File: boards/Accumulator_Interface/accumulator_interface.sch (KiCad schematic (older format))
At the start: 12 parts, among them J1 INTERNAL, J10 AIR_CTRL_18, J2 EXTERNAL, J3 AIR_CTRL, J4 IMD_LATCH, J5 DISCHARGE, J6 BMS_Master, J7 BMS, J8 TSAL/AIL, J9 IMD_LATCH, U1 RJ45_VT_AIR, U2 RJ45_VT_BMS

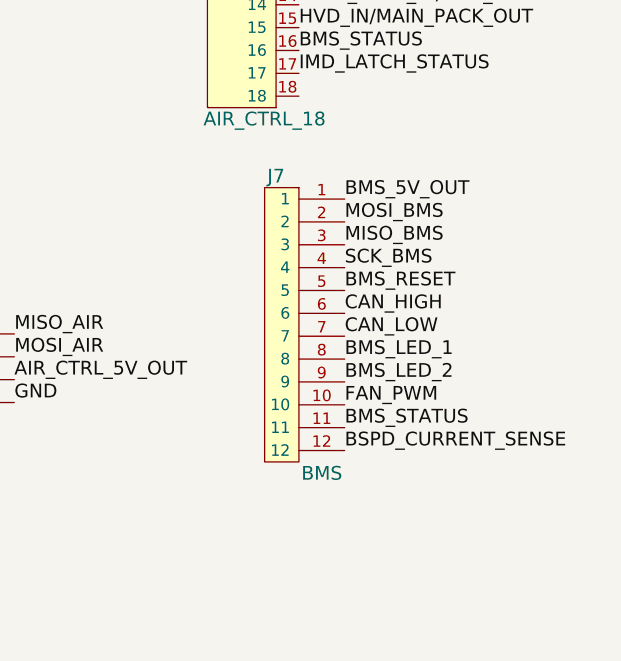
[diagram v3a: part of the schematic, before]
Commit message: added traces to accumulator
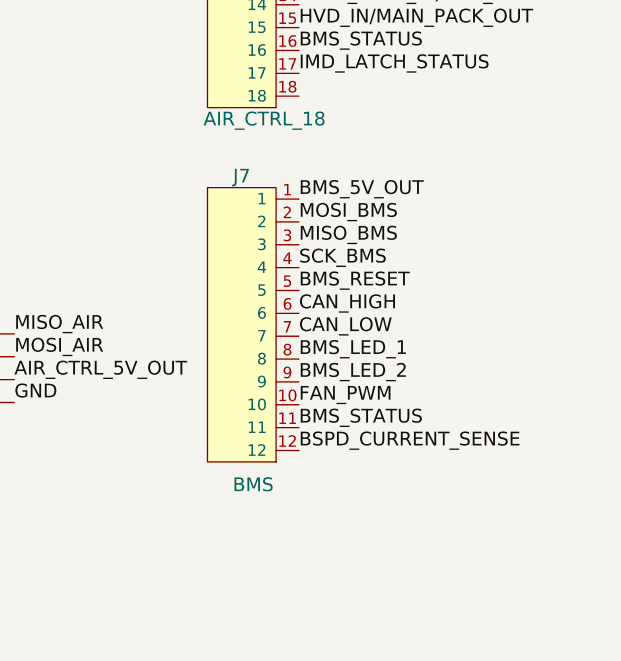
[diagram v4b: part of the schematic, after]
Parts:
- removed J7: BMS, symbol MicroFit_12
- added J7: BMS, footprints:micromatch_female_vert_12, symbol micromatch_female_TOP_ENTRY_locking_12
- J2: footprint (none) -> footprints:Ampseal_35
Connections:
- net BMS_5V_OUT: now also J7.1
- net BMS_LED_1: now also J7.8
- net BMS_LED_2: now also J7.9
- net BMS_RESET: now also J7.5
- net BMS_STATUS: now also J7.11
- net BSPD_CURRENT_SENSE: now also J7.12
- net CAN_HIGH: now also J7.6
- net CAN_LOW: now also J7.7
- net FAN_PWM: now also J7.10
- net MISO_BMS: now also J7.3
- net MOSI_BMS: now also J7.2
- net SCK_BMS: now also J7.4
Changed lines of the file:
@@
 F 0 "J2" H 750 5000 60  0000 C CNN
 F 1 "EXTERNAL" H 700 1400 60  0000 L CNN
-F 2 "" H 800 4550 60  0001 C CNN
+F 2 "footprints:Ampseal_35" H 800 4550 60  0001 C CNN
 F 3 "" H 800 4550 60  0001 C CNN
 	1    1000 3200
@@
 Text Label 5050 3850 0    60   ~ 0
 IMD_LATCH_STATUS
-Text Label 5250 4400 0    60   ~ 0
+Text Label 5050 4400 0    60   ~ 0
 BMS_5V_OUT
-Text Label 5250 4500 0    60   ~ 0
+Text Label 5050 4500 0    60   ~ 0
 MOSI_BMS
-Text Label 5250 4600 0    60   ~ 0
+Text Label 5050 4600 0    60   ~ 0
 MISO_BMS
-Text Label 5250 4700 0    60   ~ 0
+Text Label 5050 4700 0    60   ~ 0
 SCK_BMS
-Text Label 5250 4800 0    60   ~ 0
+Text Label 5050 4800 0    60   ~ 0
 BMS_RESET
-Text Label 5250 4900 0    60   ~ 0
-CAN_HIGH
-Text Label 5250 5000 0    60   ~ 0
-CAN_LOW
-Text Label 5250 5100 0    60   ~ 0
+Text Label 5050 4900 0    60   ~ 0
+CAN_HIGH
+Text Label 5050 5000 0    60   ~ 0
+CAN_LOW
+Text Label 5050 5100 0    60   ~ 0
 BMS_LED_1
-Text Label 5250 5200 0    60   ~ 0
+Text Label 5050 5200 0    60   ~ 0
 BMS_LED_2
-Text Label 5250 5300 0    60   ~ 0
-FAN_PWM
-Text Label 5250 5400 0    60   ~ 0
+Text Label 5050 5300 0    60   ~ 0
+FAN_PWM
+Text Label 5050 5400 0    60   ~ 0
 BMS_STATUS
-Text Label 5250 5500 0    60   ~ 0
+Text Label 5050 5500 0    60   ~ 0
 BSPD_CURRENT_SENSE
 Text Label 5050 1900 0    60   ~ 0
@@
 12V
 $Comp
-L MicroFit_12 J7
-U 1 1 5A7D1B20
-P 4700 4200
-F 0 "J7" H 4950 4100 60  0000 C CNN
-F 1 "BMS" H 5150 2800 60  0000 C CNN
-F 2 "" H 4700 4200 60  0001 C CNN
-F 3 "" H 4700 4200 60  0001 C CNN
-	1    4700 4200
-	1    0    0    -1
-$EndComp
+L micromatch_female_TOP_ENTRY_locking_12 J7
+U 1 1 5A825107
+P 4800 4950
+F 0 "J7" H 4800 5600 60  0000 C CNN
+F 1 "BMS" H 4850 4250 60  0000 C CNN
+F 2 "footprints:micromatch_female_vert_12" H 4700 5500 60  0001 C CNN
+F 3 "" H 4800 5600 60  0001 C CNN
+F 4 "https://www.digikey.com/product-detail/en/te-connectivity-amp-connectors/1-338068-2/A99503CT-ND/1955736" H 4900 5700 60  0001 C CNN "PurchasingLink"
+F 5 "Digi-Key" H 5000 5800 60  0001 C CNN "MFN"
+F 6 "A99503CT-ND" H 5000 6450 60  0001 C CNN "MPN"
+F 7 "Value" H 5100 6550 60  0001 C CNN "Package"
+	1    4800 4950
+	1    0    0    -1
+$EndComp

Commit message: Accu Interface updates
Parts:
- added J11: Energy_Meter_Power, footprints:Ultrafit_2, symbol Ultrafit_2
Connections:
- net 12V: now also J11.1
- net AIR_CTRL_RESET: now also U1.3 (RESET)
- net BMS_IN/IMD_LATCH_OUT: now also J10.14; no longer J10.12
- net BMS_STATUS: now also J10.12; no longer J10.16
- net GND: now also J11.2
- net HVD_IN/MAIN_PACK_OUT: now also J10.17; no longer J10.15
- net IMD_LATCH_IN/HVD_OUT: now also J10.15; no longer J10.13
- net IMD_LATCH_STATUS: now also J10.13; no longer J10.17
- net MAIN_PACK_IN/BMS_OUT: now also J10.16; no longer J10.14
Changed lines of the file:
@@
 Text Label 5050 3250 0    60   ~ 0
 AIR_CTRL_LED_2
+Text Label 5050 3550 0    60   ~ 0
+BMS_IN/IMD_LATCH_OUT
+Text Label 5050 3650 0    60   ~ 0
+IMD_LATCH_IN/HVD_OUT
+Text Label 5050 3750 0    60   ~ 0
+MAIN_PACK_IN/BMS_OUT
+Text Label 5050 3850 0    60   ~ 0
+HVD_IN/MAIN_PACK_OUT
 Text Label 5050 3350 0    60   ~ 0
-BMS_IN/IMD_LATCH_OUT
+BMS_STATUS
 Text Label 5050 3450 0    60   ~ 0
-IMD_LATCH_IN/HVD_OUT
-Text Label 5050 3550 0    60   ~ 0
-MAIN_PACK_IN/BMS_OUT
-Text Label 5050 3650 0    60   ~ 0
-HVD_IN/MAIN_PACK_OUT
-Text Label 5050 3750 0    60   ~ 0
-BMS_STATUS
-Text Label 5050 3850 0    60   ~ 0
 IMD_LATCH_STATUS
 Text Label 5050 4400 0    60   ~ 0
@@
 	1    0    0    -1
 $EndComp
+$Comp
+L Ultrafit_2 J11
+U 1 1 5A864268
+P 3780 4425
+F 0 "J11" H 3780 4575 60  0000 C CNN
+F 1 "Energy_Meter_Power" H 3880 4275 60  0000 C CNN
+F 2 "footprints:Ultrafit_2" H 3680 4475 60  0001 C CNN
+F 3 "" H 3780 4575 60  0001 C CNN
+F 4 "https://www.digikey.com/product-detail/en/molex-llc/1722861102/WM11570-ND/5344267" H 3880 4675 60  0001 C CNN "PurchasingLink"
+F 5 "Digi-Key" H 3980 4775 60  0001 C CNN "MFN"
+F 6 "WM11570-ND" H 4080 4875 60  0001 C CNN "MPN"
+F 7 "Value" H 4180 4975 60  0001 C CNN "Package"
+	1    3780 4425
+	1    0    0    -1
+$EndComp
+Text Label 2475 5190 2    60   ~ 0
+AIR_CTRL_RESET
+Text Label 4030 4375 0    60   ~ 0
+12V
+Text Label 4030 4475 0    60   ~ 0
+GND
 $EndSCHEMATC

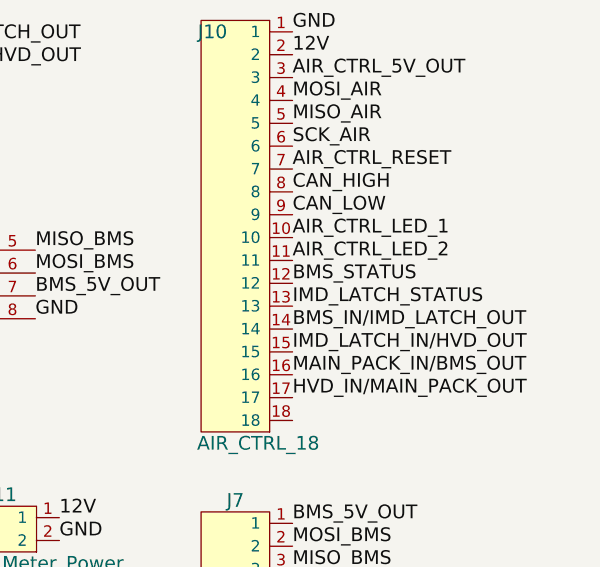
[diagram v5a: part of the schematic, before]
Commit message: Modified layout for accumulator board.
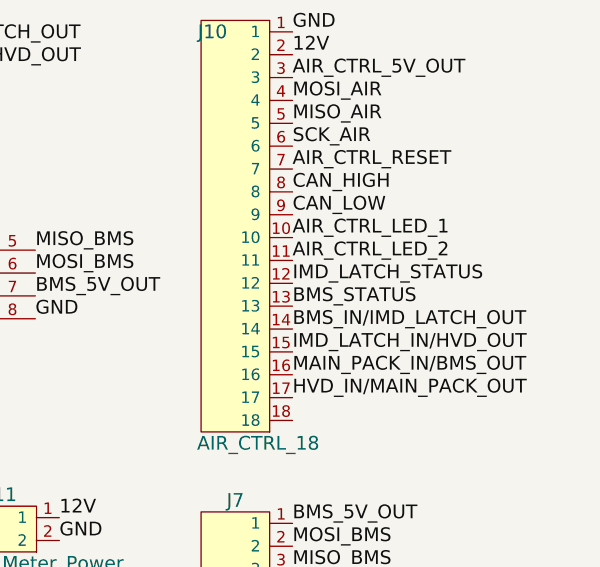
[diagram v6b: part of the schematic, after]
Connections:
- net BMS_STATUS: now also J10.13; no longer J10.12
- net IMD_LATCH_STATUS: now also J10.12; no longer J10.13
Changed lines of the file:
@@
 Text Label 5050 3850 0    60   ~ 0
 HVD_IN/MAIN_PACK_OUT
+Text Label 5050 3450 0    60   ~ 0
+BMS_STATUS
 Text Label 5050 3350 0    60   ~ 0
-BMS_STATUS
-Text Label 5050 3450 0    60   ~ 0
 IMD_LATCH_STATUS
 Text Label 5050 4400 0    60   ~ 0

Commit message: Accum Update
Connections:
- net 12V: now also J2.16, J2.17, J2.7, J2.8, J2.9
- net CAN_HIGH: now also J2.20, J2.21
- net CAN_LOW: now also J2.18, J2.19
- net FAN_12V: no longer J2.7, J2.8, J2.9
- net FAN_GND: no longer J2.4, J2.5, J2.6
- net GND: now also J2.22, J2.23, J2.4, J2.5, J2.6
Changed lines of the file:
@@
 Text Label 1200 1700 0    60   ~ 0
 GND
-Text Label 1200 1800 0    60   ~ 0
+Text Label 2020 1760 0    60   ~ 0
 FAN_GND
-Text Label 1200 1900 0    60   ~ 0
+Text Label 2020 1860 0    60   ~ 0
 FAN_GND
-Text Label 1200 2000 0    60   ~ 0
+Text Label 2020 1960 0    60   ~ 0
 FAN_GND
-Text Label 1200 2100 0    60   ~ 0
+Text Label 2020 2060 0    60   ~ 0
 FAN_12V
-Text Label 1200 2200 0    60   ~ 0
+Text Label 2020 2160 0    60   ~ 0
 FAN_12V
-Text Label 1200 2300 0    60   ~ 0
+Text Label 2020 2260 0    60   ~ 0
 FAN_12V
 Text Label 1200 2400 0    60   ~ 0
@@
 Text Label 4030 4475 0    60   ~ 0
 GND
+Text Label 1200 1800 0    60   ~ 0
+GND
+Text Label 1200 1900 0    60   ~ 0
+GND
+Text Label 1200 2000 0    60   ~ 0
+GND
+Text Label 1200 2100 0    60   ~ 0
+12V
+Text Label 1200 2200 0    60   ~ 0
+12V
+Text Label 1200 2300 0    60   ~ 0
+12V
+Text Label 1200 3000 0    60   ~ 0
+12V
+Text Label 1200 3100 0    60   ~ 0
+12V
+Text Label 1200 3600 0    60   ~ 0
+GND
+Text Label 1200 3700 0    60   ~ 0
+GND
+Text Label 1200 3500 0    60   ~ 0
+CAN_HIGH
+Text Label 1200 3300 0    60   ~ 0
+CAN_LOW
+Text Label 1200 3400 0    60   ~ 0
+CAN_HIGH
+Text Label 1200 3200 0    60   ~ 0
+CAN_LOW
 $EndSCHEMATC

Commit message: added a cad for the board
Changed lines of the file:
@@
 	1    0    0    -1
 $EndComp
-Entry Wire Line
-	6200 850  6300 950
 Text Label 3250 1200 0    60   ~ 0
 GND
